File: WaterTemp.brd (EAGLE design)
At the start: 95 x 25 mm, 24 parts, among them J1 2X6-HEADERS, U3 M24C02-WMN6TP

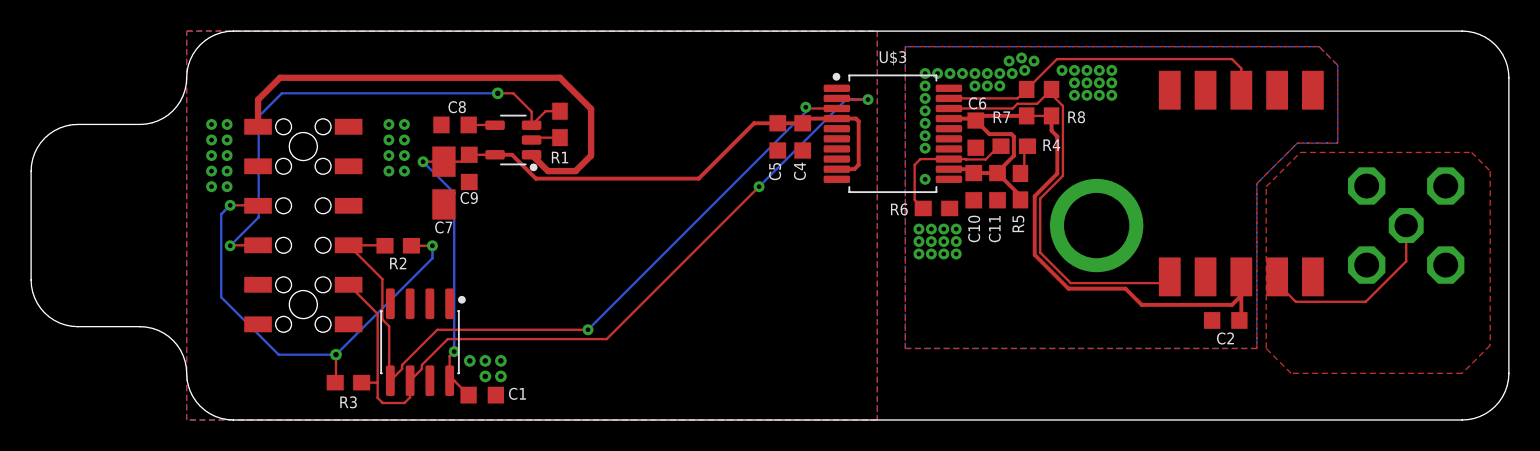
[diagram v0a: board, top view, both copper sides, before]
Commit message: Quadfurcated modules into individual files, migrated to new footprint, added module tags to tabs, moved Weather programming header.
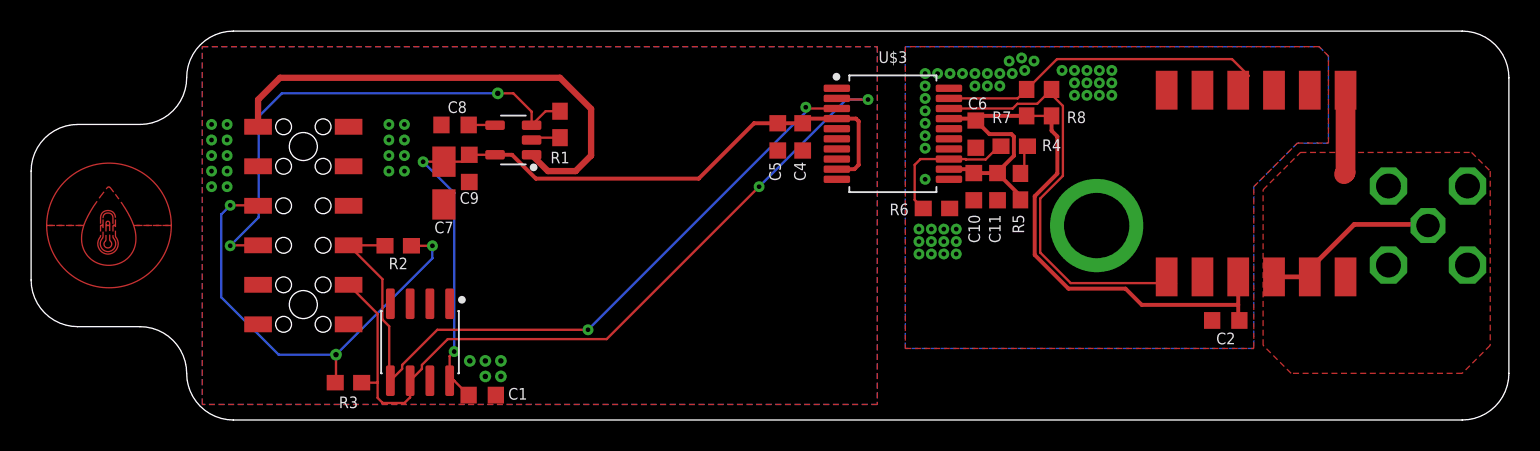
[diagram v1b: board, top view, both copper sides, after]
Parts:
- U$2: value ATLAS10P -> ATLAS12P; device Conservify:ATLAS-10P -> Conservify:ATLAS-12P
- moved U$1 1.40 mm to (79.8, 12.5)
- moved U$2 0.80 mm to (69.0, 15.2)
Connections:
- net I3V3: now also U$2.VCC; no longer U$2.PAD3
- net IGND: now also U$2.GND; no longer U$2.PAD6
- net ISCL: now also U$2.SCL; no longer U$2.PAD8
- net ISDA: now also U$2.SDA; no longer U$2.PAD1
- net N$2: now also U$2.PRB1, U$2.PRB2; no longer U$2.PAD4
- net PG: now also U$2.PRB3, U$2.PRB4; no longer U$2.PAD5
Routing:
- net PG: track 0.00 -> 5.44 mm
- net I3V3: track 46.8 -> 45.9 mm
- net ISDA: track 27.8 -> 28.8 mm
- net N$2: track 12.6 -> 11.6 mm
- added copper zone on layer 1, net GND1
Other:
- board text added: "THIS SIDE DOWN"
